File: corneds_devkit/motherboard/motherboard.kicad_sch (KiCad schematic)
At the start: 0 parts

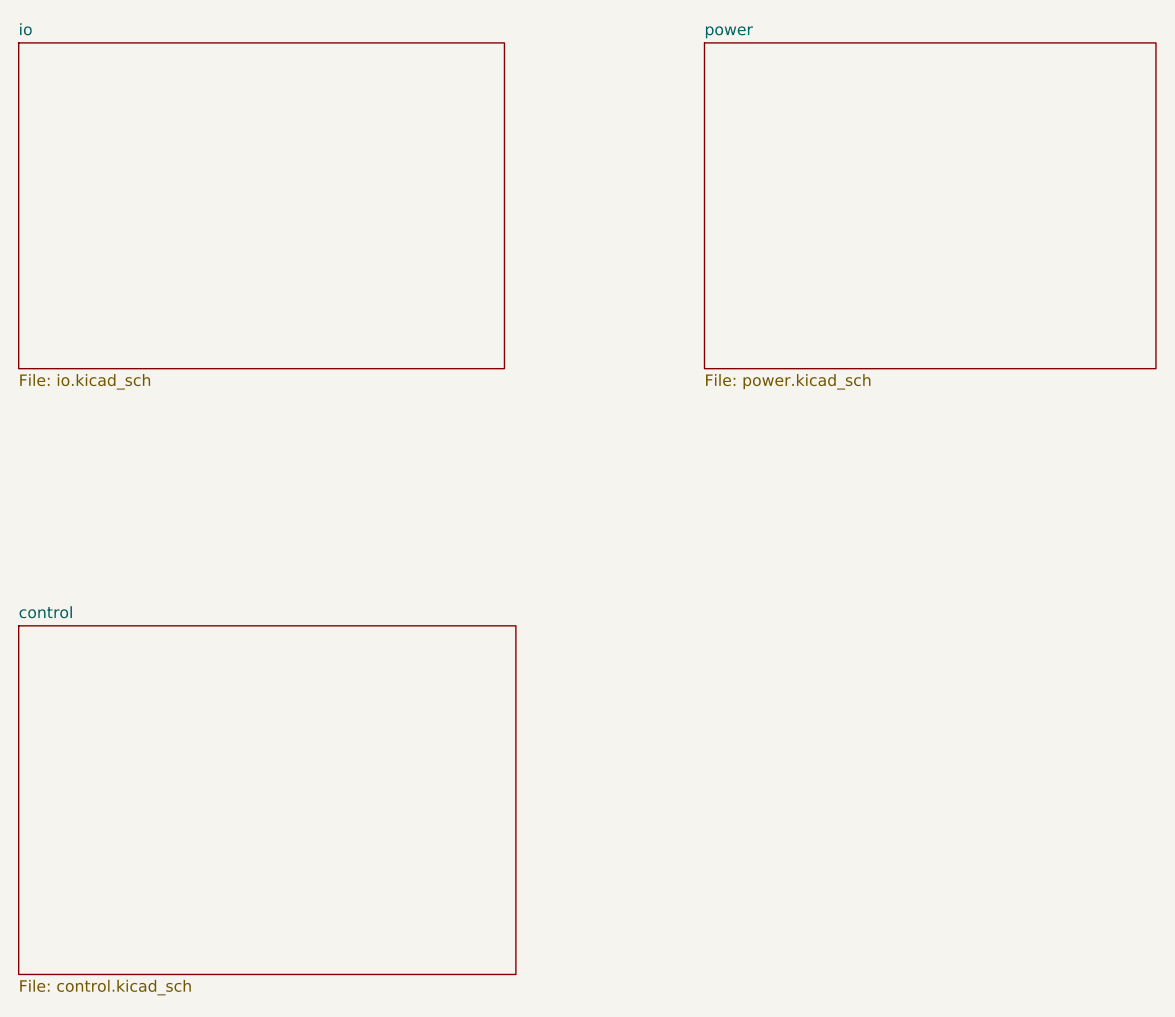
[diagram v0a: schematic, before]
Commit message: ordered devkit rev A
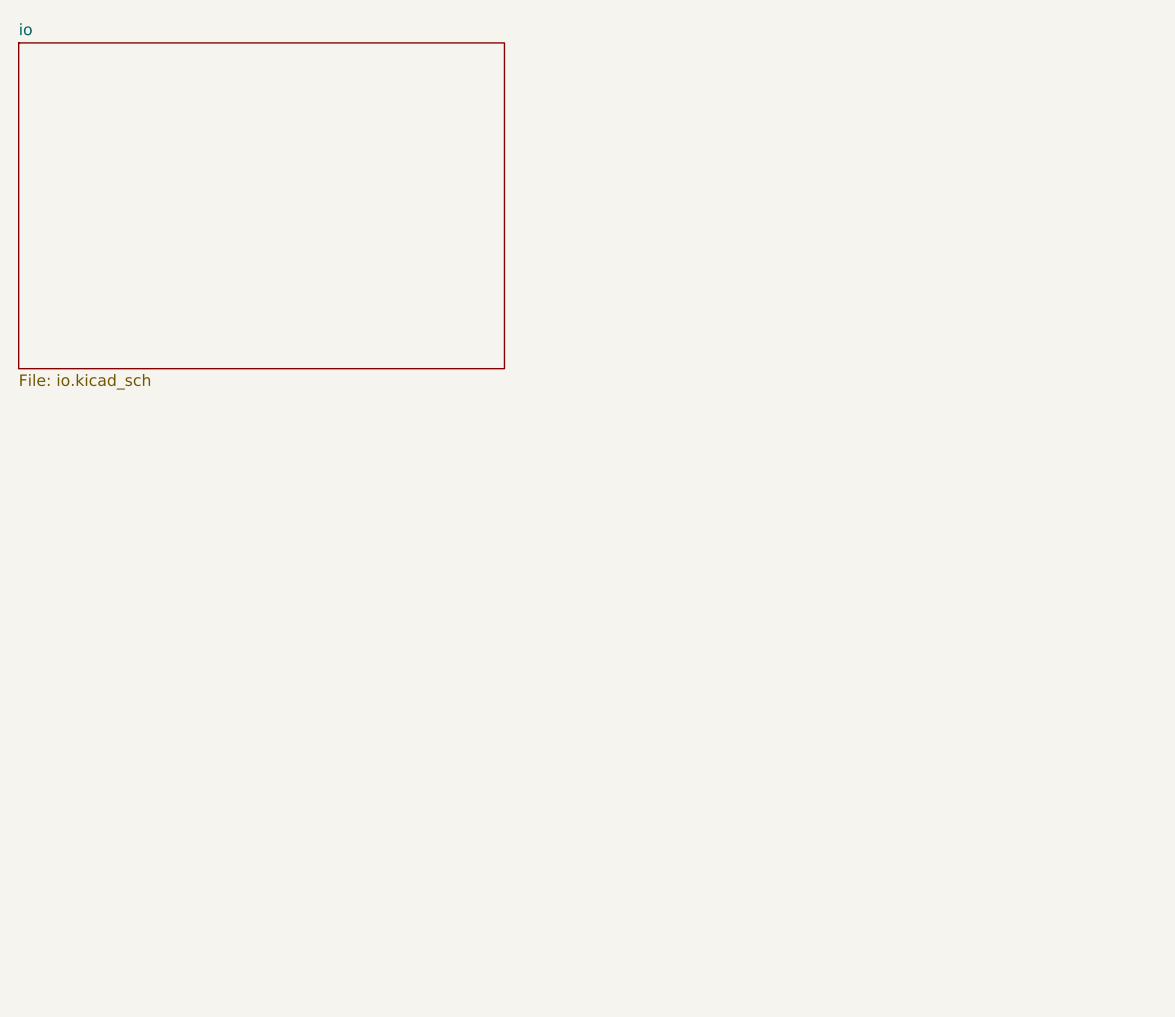
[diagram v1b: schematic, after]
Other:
- removed sheet control
- removed sheet power
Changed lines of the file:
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@@
 	(paper "A4")
-	(sheet
-		(at 102.87 22.225)
-		(size 50.165 36.195)
-		(fields_autoplaced yes)
-		(stroke
-			(width 0.1524)
-			(type solid)
-		)
-		(fill
-			(color 0 0 0 0.0000)
-		)
-		(property "Sheetname" "power"
-			(at 102.87 21.5134 0)
-			(effects
-				(font
-					(size 1.27 1.27)
-				)
-				(justify left bottom)
-			)
-		)
-		(property "Sheetfile" "power.kicad_sch"
-			(at 102.87 59.0046 0)
-			(effects
-				(font
-					(size 1.27 1.27)
-				)
-				(justify left top)
-			)
-		)
-		(instances
-			(project "motherboard"
-				(path "/e62bdc8c-b7a7-4fbc-b4c4-d3d1c2fc1d9d"
-					(page "3")
-				)
-			)
-		)
-	)
 	(sheet
 		(at 26.67 22.225)
@@
 				)
 			)
-		)
-	)
-	(sheet
-		(at 26.67 86.995)
-		(size 55.245 38.735)
-		(fields_autoplaced yes)
-		(stroke
-			(width 0.1524)
-			(type solid)
-		)
-		(fill
-			(color 0 0 0 0.0000)
-		)
-		(property "Sheetname" "control"
-			(at 26.67 86.2834 0)
-			(effects
-				(font
-					(size 1.27 1.27)
-				)
-				(justify left bottom)
-			)
-		)
-		(property "Sheetfile" "control.kicad_sch"
-			(at 26.67 126.3146 0)
-			(effects
-				(font
-					(size 1.27 1.27)
-				)
-				(justify left top)
-			)
-		)
-		(instances
-			(project "motherboard"
-				(path "/e62bdc8c-b7a7-4fbc-b4c4-d3d1c2fc1d9d"
-					(page "4")
-				)
-			)
